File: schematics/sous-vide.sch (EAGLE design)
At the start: 27 parts, among them IC1 MEGA32-P, Q2 BC517, Q3 BC517

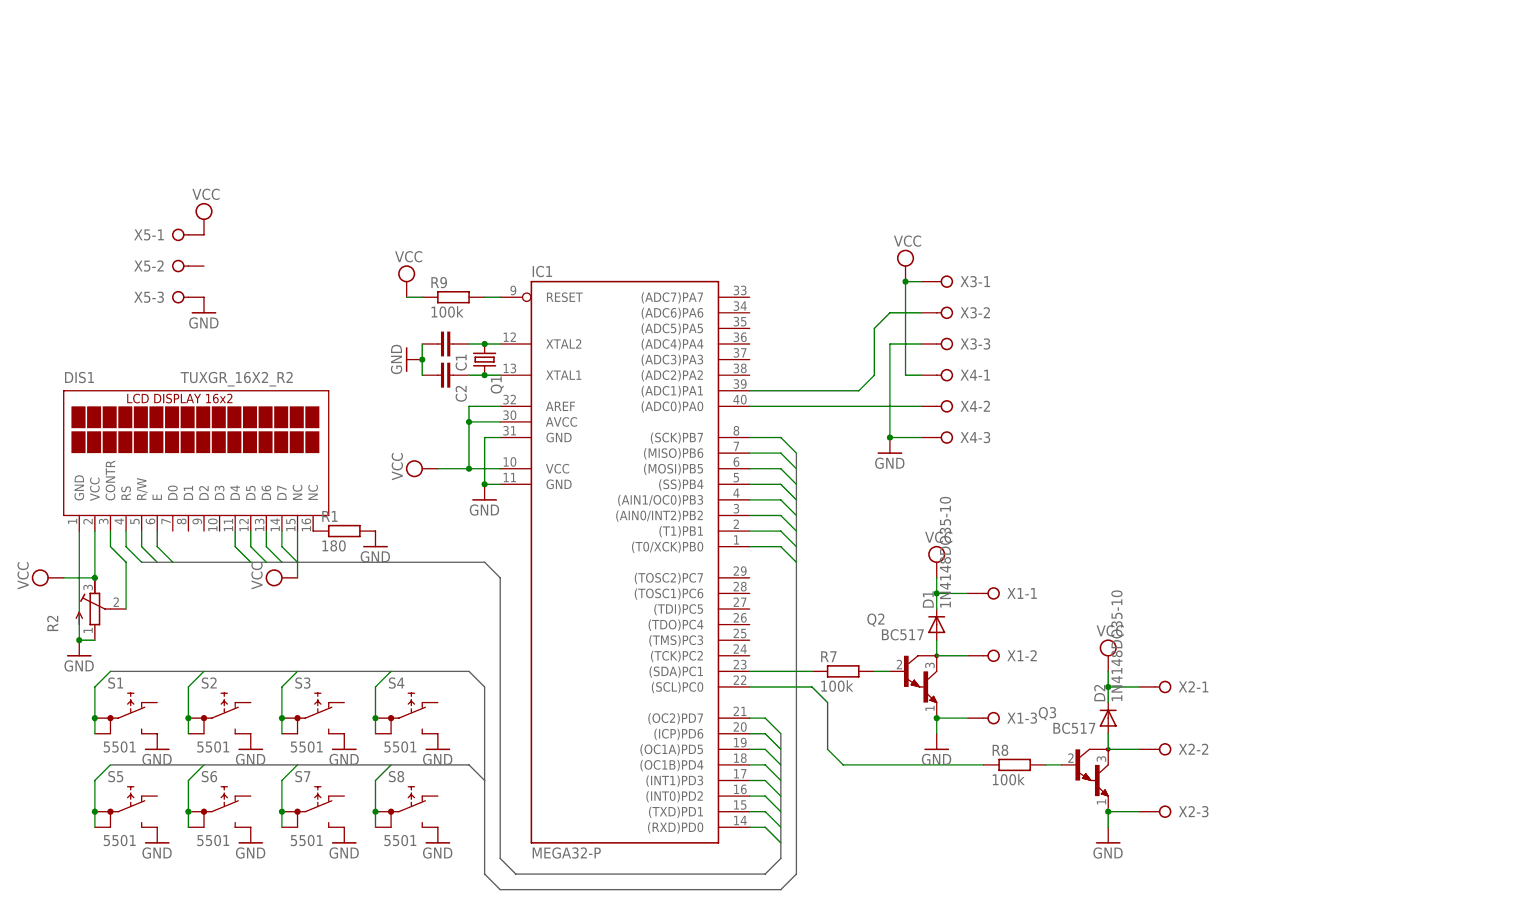
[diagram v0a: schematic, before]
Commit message: Electronic schema and board updated
Created an 8x8 cm board for cpu, display and buttons.
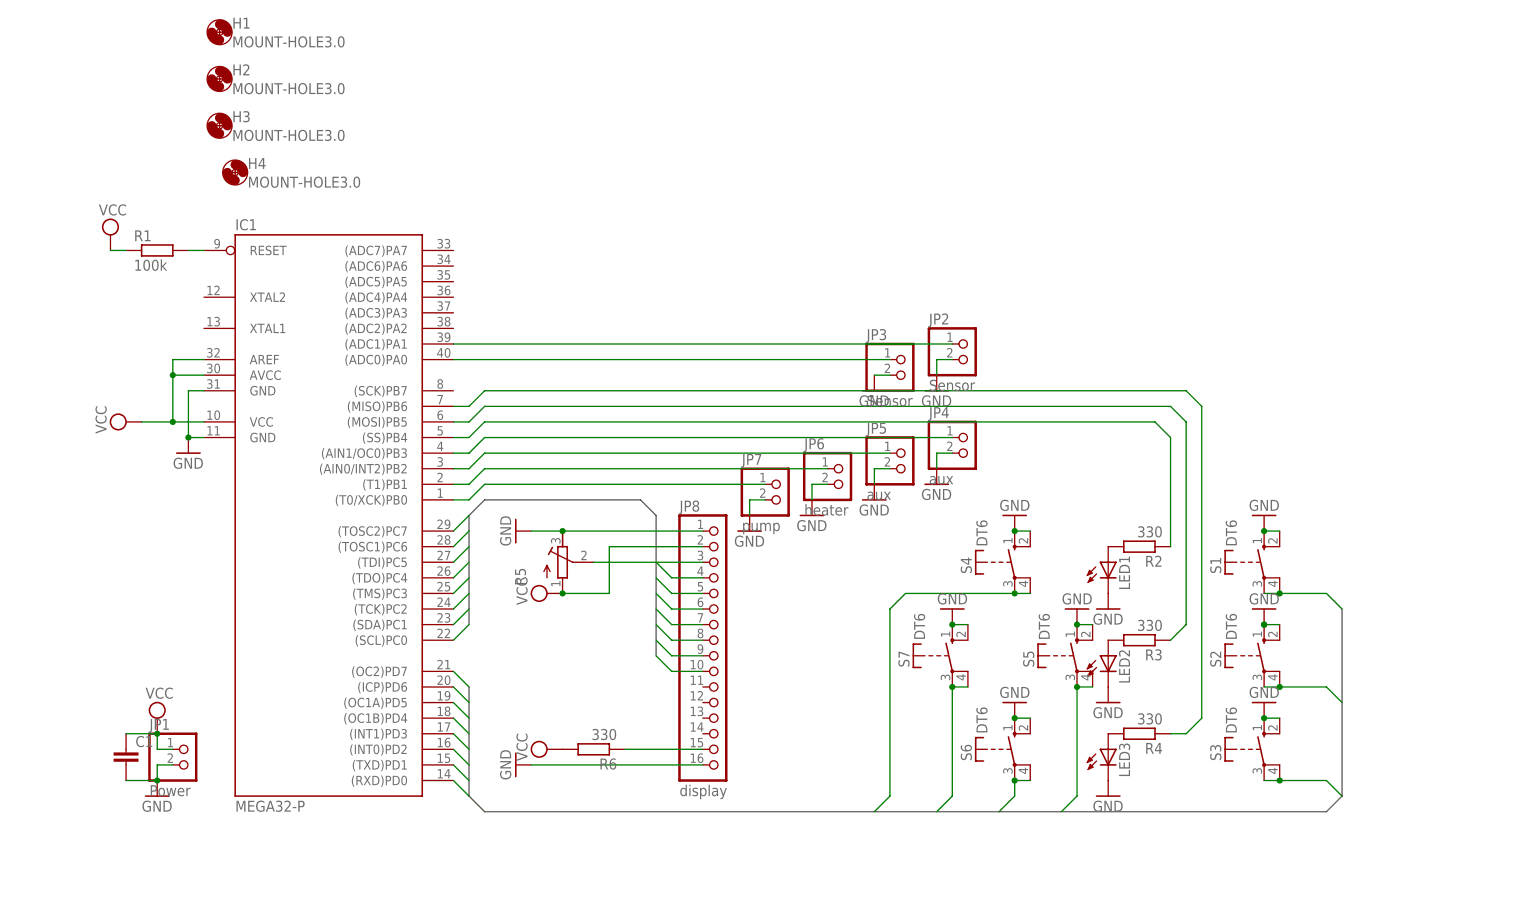
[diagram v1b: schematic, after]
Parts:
- removed C2: (no value), rcl:C-EU025-024X044
- removed D1, D2: 1N4148DO35-10, diode:1N4148DO35-10
- removed DIS1: TUXGR_16X2_R2, display-lcd:TUXGR_16X2_R2
- removed Q1: (no value), crystal:CRYSTALHC49S
- removed Q2, Q3: BC517, transistor-npn:BC517
- removed R7, R8, R9: 100k, rcl:R-EU_0207/2V
- removed S8: 5501, switch:5501
- removed X1, X2, X3, X4, X5: (no value), con-wago-508:W237-3E
- added H1, H2, H3, H4: MOUNT-HOLE3.0, holes:MOUNT-HOLE3.0
- added JP1: Power, pinhead:PINHD-1X2
- added JP2, JP3: Sensor, pinhead:PINHD-1X2
- added JP4, JP5: aux, pinhead:PINHD-1X2
- added JP6: heater, pinhead:PINHD-1X2
- added JP7: pump, pinhead:PINHD-1X2
- added JP8: display, pinhead:PINHD-1X16
- added LED1, LED2, LED3: (no value), led:LED3MM
- added R3, R4, R6: 330, rcl:R-EU_0207/2V
- added R5: (no value), resistor:R-TRIMM3339P
- C1: device rcl:C-EU025-024X044 -> resistor:C-EU025-025X050
- R1: value 180 -> 100k
- R2: value (none) -> 330; device resistor:R-TRIMM3339P -> rcl:R-EU_0207/2V
- S1, S2, S3, S4, S5, S6, S7: value 5501 -> DT6; device switch:5501 -> switch-misc:DT6
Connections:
- removed net SWITCH0: IC1.(T0/XCK)PB0, S1.1A, S1.1B
- removed net SWITCH1: IC1.(T1)PB1, S2.1A, S2.1B
- removed net SWITCH2: IC1.(AIN0/INT2)PB2, S3.1A, S3.1B
- removed net SWITCH3: IC1.(AIN1/OC0)PB3, S4.1A, S4.1B
- removed net SWITCH4: IC1.(SS)PB4, S5.1A, S5.1B
- removed net SWITCH5: IC1.(MOSI)PB5, S6.1A, S6.1B
- removed net SWITCH6: IC1.(MISO)PB6, S7.1A, S7.1B
- removed net SWITCH7: IC1.(SCK)PB7, S8.1A, S8.1B
- new net BUTTON0: IC1.(RXD)PD0, S1.P, S1.P@1
- new net BUTTON1: IC1.(TXD)PD1, S2.P, S2.P@1
- new net BUTTON2: IC1.(INT0)PD2, S3.P, S3.P@1
- new net BUTTON3: IC1.(INT1)PD3, S4.P, S4.P@1
- new net BUTTON4: IC1.(OC1B)PD4, S5.P, S5.P@1
- new net BUTTON5: IC1.(OC1A)PD5, S6.P, S6.P@1
- new net BUTTON6: IC1.(ICP)PD6, S7.P, S7.P@1
- new net BUTTON7: IC1.(OC2)PD7
- new net N$14: JP8.3, R5.S
- new net N$15: JP8.15, R6.1
- net DISPLAY0: now also IC1.(SCL)PC0; no longer DIS1.RS, IC1.(RXD)PD0
- net DISPLAY1: now also IC1.(SDA)PC1, JP8.4; no longer DIS1.R/W, IC1.(TXD)PD1
- net DISPLAY2: now also IC1.(TCK)PC2, JP8.5; no longer DIS1.E, IC1.(INT0)PD2
- net DISPLAY3: now also IC1.(TMS)PC3, JP8.6; no longer DIS1.D4, IC1.(INT1)PD3
- net DISPLAY4: now also IC1.(TDO)PC4, JP8.7; no longer DIS1.D5, IC1.(OC1B)PD4
- net DISPLAY5: now also IC1.(TDI)PC5, JP8.8; no longer DIS1.D6, IC1.(OC1A)PD5
- net DISPLAY6: now also IC1.(TOSC1)PC6, JP8.9; no longer DIS1.D7, IC1.(ICP)PD6
- net DISPLAY7: now also IC1.(TOSC2)PC7, JP8.10; no longer IC1.(OC2)PD7
- net GND: now also JP1.2, JP2.2, JP3.2, JP4.2, JP5.2, JP6.2, JP7.2, JP8.1, JP8.16, LED1.C, LED2.C, LED3.C, R5.A, S1.S, S1.S@1, S2.S, S2.S@1, S3.S, S3.S@1, S4.S, S4.S@1, S5.S, S5.S@1, S6.S, S6.S@1, S7.S, S7.S@1; no longer C2.2, DIS1.GND, Q2.E, Q3.E, R1.2, R2.E, S1.NO, S2.NO, S3.NO, S4.NO, S5.NO, S6.NO, S7.NO, S8.NO, X1-3.KL, X2-3.KL, X3-3.KL, X4-3.KL, X5-3.KL
- net N$1: now also IC1.(T0/XCK)PB0, JP7.1; no longer C1.1, IC1.XTAL2, Q1.1
- net N$10: now also IC1.(SS)PB4, R2.1; no longer Q3.B, R8.2
- net N$11: now also IC1.(MOSI)PB5, R3.1; no longer IC1.(ADC1)PA1, X3-2.KL
- net N$12: now also JP3.1; no longer X4-2.KL
- net N$13: now also IC1.(MISO)PB6, R4.1; no longer DIS1.CONTR, R2.S
- net N$2: now also IC1.(T1)PB1, JP6.1; no longer C2.1, IC1.XTAL1, Q1.2
- net N$3: now also R1.2; no longer R9.2
- net N$4: now also IC1.(AIN0/INT2)PB2, JP5.1; no longer D2.A, Q3.C, X2-2.KL
- net N$5: now also IC1.(AIN1/OC0)PB3, JP4.1; no longer DIS1.NC@2, R1.1
- net N$6: now also IC1.(ADC1)PA1, JP2.1; no longer IC1.(SCL)PC0, R8.1
- net N$7: now also LED3.A, R4.2; no longer IC1.(SDA)PC1, R7.1
- net N$8: now also LED2.A, R3.2; no longer Q2.B, R7.2
- net N$9: now also LED1.A, R2.2; no longer D1.A, Q2.C, X1-2.KL
- net VCC: now also C1.1, JP1.1, JP8.2, R1.1, R5.E, R6.2; no longer D1.C, D2.C, DIS1.NC@1, DIS1.VCC, R2.A, R9.1, X1-1.KL, X2-1.KL, X3-1.KL, X4-1.KL, X5-1.KL
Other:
- moved on the sheet: C1, IC1, R1

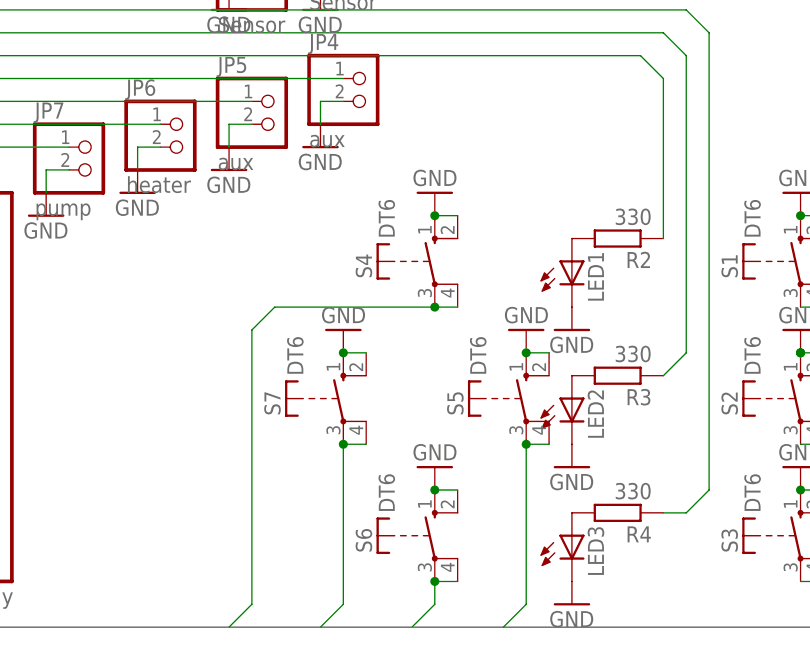
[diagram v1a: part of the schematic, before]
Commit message: Optimized PCB
Optimized PCB with easier traces for buttons.
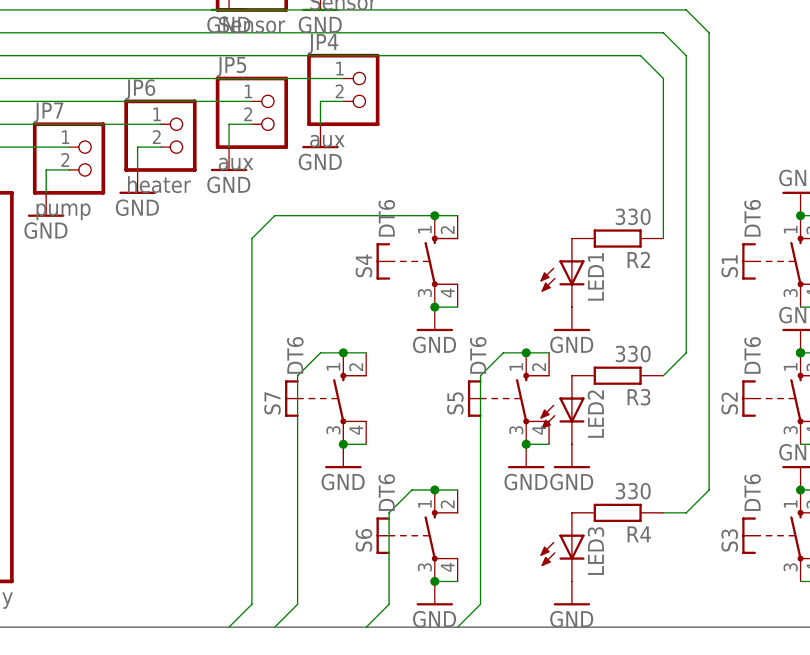
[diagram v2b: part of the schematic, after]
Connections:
- net BUTTON3: now also S4.S, S4.S@1; no longer S4.P, S4.P@1
- net BUTTON4: now also S5.S, S5.S@1; no longer S5.P, S5.P@1
- net BUTTON5: now also S6.S, S6.S@1; no longer S6.P, S6.P@1
- net BUTTON6: now also S7.S, S7.S@1; no longer S7.P, S7.P@1
- net GND: now also S4.P, S4.P@1, S5.P, S5.P@1, S6.P, S6.P@1, S7.P, S7.P@1; no longer S4.S, S4.S@1, S5.S, S5.S@1, S6.S, S6.S@1, S7.S, S7.S@1
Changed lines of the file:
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@@
 <part name="GND2" library="supply1" deviceset="GND" device=""/>
 <part name="GND3" library="supply1" deviceset="GND" device=""/>
-<part name="GND4" library="supply1" deviceset="GND" device=""/>
-<part name="GND5" library="supply1" deviceset="GND" device=""/>
-<part name="GND6" library="supply1" deviceset="GND" device=""/>
-<part name="GND7" library="supply1" deviceset="GND" device=""/>
 <part name="GND8" library="supply1" deviceset="GND" device=""/>
 <part name="JP7" library="pinhead" deviceset="PINHD-1X2" device="" value="pump"/>
@@
 <part name="H3" library="holes" deviceset="MOUNT-HOLE" device="3.0"/>
 <part name="H4" library="holes" deviceset="MOUNT-HOLE" device="3.0"/>
+<part name="GND4" library="supply1" deviceset="GND" device=""/>
+<part name="GND5" library="supply1" deviceset="GND" device=""/>
+<part name="GND6" library="supply1" deviceset="GND" device=""/>
+<part name="GND7" library="supply1" deviceset="GND" device=""/>
 </parts>
 <sheets>
@@
 <instance part="GND2" gate="1" x="190.5" y="38.1" rot="R180"/>
 <instance part="GND3" gate="1" x="190.5" y="22.86" rot="R180"/>
-<instance part="GND4" gate="1" x="149.86" y="53.34" rot="R180"/>
-<instance part="GND5" gate="1" x="160.02" y="38.1" rot="R180"/>
-<instance part="GND6" gate="1" x="149.86" y="22.86" rot="R180"/>
-<instance part="GND7" gate="1" x="139.7" y="38.1" rot="R180"/>
 <instance part="GND8" gate="1" x="15.24" y="63.5"/>
 <instance part="JP7" gate="G$1" x="111.76" y="55.88"/>
@@
 <instance part="H3" gate="G$1" x="20.32" y="116.84"/>
 <instance part="H4" gate="G$1" x="22.86" y="109.22"/>
+<instance part="GND4" gate="1" x="149.86" y="38.1"/>
+<instance part="GND5" gate="1" x="139.7" y="22.86"/>
+<instance part="GND6" gate="1" x="160.02" y="22.86"/>
+<instance part="GND7" gate="1" x="149.86" y="7.62"/>
 </instances>
 <busses>
@@
 </segment>
 <segment>
-<pinref part="S4" gate="1" pin="S"/>
-<pinref part="GND4" gate="1" pin="GND"/>
-<pinref part="S4" gate="1" pin="S@1"/>
-<wire x1="152.4" y1="50.8" x2="149.86" y2="50.8" width="0.1524" layer="91"/>
-<junction x="149.86" y="50.8"/>
-</segment>
-<segment>
-<pinref part="S5" gate="1" pin="S"/>
-<pinref part="GND5" gate="1" pin="GND"/>
-<junction x="160.02" y="35.56"/>
-<pinref part="S5" gate="1" pin="S@1"/>
-<wire x1="160.02" y1="35.56" x2="162.56" y2="35.56" width="0.1524" layer="91"/>
-</segment>
-<segment>
-<pinref part="S6" gate="1" pin="S"/>
-<pinref part="GND6" gate="1" pin="GND"/>
-<junction x="149.86" y="20.32"/>
-<pinref part="S6" gate="1" pin="S@1"/>
-<wire x1="149.86" y1="20.32" x2="152.4" y2="20.32" width="0.1524" layer="91"/>
-</segment>
-<segment>
-<pinref part="S7" gate="1" pin="S"/>
-<pinref part="GND7" gate="1" pin="GND"/>
-<junction x="139.7" y="35.56"/>
-<pinref part="S7" gate="1" pin="S@1"/>
-<wire x1="139.7" y1="35.56" x2="142.24" y2="35.56" width="0.1524" layer="91"/>
-</segment>
-<segment>
 <pinref part="IC1" gate="G$1" pin="GND@1"/>
 <wire x1="17.78" y1="73.66" x2="15.24" y2="73.66" width="0.1524" layer="91"/>
@@
 <pinref part="GND20" gate="1" pin="GND"/>
 <wire x1="99.06" y1="12.7" x2="71.12" y2="12.7" width="0.1524" layer="91"/>
+</segment>
+<segment>
+<pinref part="S4" gate="1" pin="P"/>
+<pinref part="GND4" gate="1" pin="GND"/>
+<pinref part="S4" gate="1" pin="P@1"/>
+<wire x1="152.4" y1="40.64" x2="149.86" y2="40.64" width="0.1524" layer="91"/>
+<junction x="149.86" y="40.64"/>
+</segment>
+<segment>
+<pinref part="S7" gate="1" pin="P"/>
+<pinref part="GND5" gate="1" pin="GND"/>
+<pinref part="S7" gate="1" pin="P@1"/>
+<wire x1="142.24" y1="25.4" x2="139.7" y2="25.4" width="0.1524" layer="91"/>
+<junction x="139.7" y="25.4"/>
+</segment>
+<segment>
+<pinref part="S5" gate="1" pin="P"/>
+<pinref part="GND6" gate="1" pin="GND"/>
+<pinref part="S5" gate="1" pin="P@1"/>
+<wire x1="162.56" y1="25.4" x2="160.02" y2="25.4" width="0.1524" layer="91"/>
+<junction x="160.02" y="25.4"/>
+</segment>
+<segment>
+<pinref part="S6" gate="1" pin="P"/>
+<pinref part="GND7" gate="1" pin="GND"/>
+<pinref part="S6" gate="1" pin="P@1"/>
+<wire x1="152.4" y1="10.16" x2="149.86" y2="10.16" width="0.1524" layer="91"/>
+<junction x="149.86" y="10.16"/>
 </segment>
 </net>
@@
 </segment>
 <segment>
-<wire x1="147.32" y1="5.08" x2="149.86" y2="7.62" width="0.1524" layer="91"/>
-<pinref part="S6" gate="1" pin="P"/>
-<wire x1="149.86" y1="7.62" x2="149.86" y2="10.16" width="0.1524" layer="91"/>
-<pinref part="S6" gate="1" pin="P@1"/>
-<wire x1="152.4" y1="10.16" x2="149.86" y2="10.16" width="0.1524" layer="91"/>
-<junction x="149.86" y="10.16"/>
+<wire x1="142.24" y1="5.08" x2="144.78" y2="7.62" width="0.1524" layer="91"/>
+<wire x1="144.78" y1="7.62" x2="144.78" y2="17.78" width="0.1524" layer="91"/>
+<wire x1="144.78" y1="17.78" x2="147.32" y2="20.32" width="0.1524" layer="91"/>
+<pinref part="S6" gate="1" pin="S@1"/>
+<wire x1="147.32" y1="20.32" x2="149.86" y2="20.32" width="0.1524" layer="91"/>
+<pinref part="S6" gate="1" pin="S"/>
+<junction x="149.86" y="20.32"/>
+<wire x1="149.86" y1="20.32" x2="152.4" y2="20.32" width="0.1524" layer="91"/>
 </segment>
 </net>
@@
 </segment>
 <segment>
-<wire x1="137.16" y1="5.08" x2="139.7" y2="7.62" width="0.1524" layer="91"/>
-<pinref part="S7" gate="1" pin="P"/>
-<wire x1="139.7" y1="7.62" x2="139.7" y2="25.4" width="0.1524" layer="91"/>
-<pinref part="S7" gate="1" pin="P@1"/>
-<wire x1="139.7" y1="25.4" x2="142.24" y2="25.4" width="0.1524" layer="91"/>
-<junction x="139.7" y="25.4"/>
+<wire x1="132.08" y1="5.08" x2="134.62" y2="7.62" width="0.1524" layer="91"/>
+<wire x1="134.62" y1="7.62" x2="134.62" y2="33.02" width="0.1524" layer="91"/>
+<wire x1="134.62" y1="33.02" x2="137.16" y2="35.56" width="0.1524" layer="91"/>
+<pinref part="S7" gate="1" pin="S@1"/>
+<wire x1="137.16" y1="35.56" x2="139.7" y2="35.56" width="0.1524" layer="91"/>
+<pinref part="S7" gate="1" pin="S"/>
+<junction x="139.7" y="35.56"/>
+<wire x1="139.7" y1="35.56" x2="142.24" y2="35.56" width="0.1524" layer="91"/>
 </segment>
 </net>
@@
 </segment>
 <segment>
-<wire x1="157.48" y1="5.08" x2="160.02" y2="7.62" width="0.1524" layer="91"/>
-<wire x1="160.02" y1="7.62" x2="160.02" y2="25.4" width="0.1524" layer="91"/>
-<pinref part="S5" gate="1" pin="P@1"/>
-<pinref part="S5" gate="1" pin="P"/>
-<junction x="160.02" y="25.4"/>
-<wire x1="160.02" y1="25.4" x2="162.56" y2="25.4" width="0.1524" layer="91"/>
+<wire x1="152.4" y1="5.08" x2="154.94" y2="7.62" width="0.1524" layer="91"/>
+<wire x1="154.94" y1="7.62" x2="154.94" y2="33.02" width="0.1524" layer="91"/>
+<wire x1="154.94" y1="33.02" x2="157.48" y2="35.56" width="0.1524" layer="91"/>
+<pinref part="S5" gate="1" pin="S@1"/>
+<wire x1="157.48" y1="35.56" x2="160.02" y2="35.56" width="0.1524" layer="91"/>
+<pinref part="S5" gate="1" pin="S"/>
+<junction x="160.02" y="35.56"/>
+<wire x1="160.02" y1="35.56" x2="162.56" y2="35.56" width="0.1524" layer="91"/>
 </segment>
 </net>
@@
 </segment>
 <segment>
-<wire x1="129.54" y1="38.1" x2="132.08" y2="40.64" width="0.1524" layer="91"/>
-<pinref part="S4" gate="1" pin="P"/>
-<wire x1="132.08" y1="40.64" x2="149.86" y2="40.64" width="0.1524" layer="91"/>
-<pinref part="S4" gate="1" pin="P@1"/>
-<wire x1="152.4" y1="40.64" x2="149.86" y2="40.64" width="0.1524" layer="91"/>
-<junction x="149.86" y="40.64"/>
-<wire x1="129.54" y1="38.1" x2="129.54" y2="7.62" width="0.1524" layer="91"/>
+<wire x1="129.54" y1="48.26" x2="129.54" y2="7.62" width="0.1524" layer="91"/>
 <wire x1="129.54" y1="7.62" x2="127" y2="5.08" width="0.1524" layer="91"/>
-</segment>
-</net>
+<pinref part="S4" gate="1" pin="S@1"/>
+<pinref part="S4" gate="1" pin="S"/>
+<wire x1="152.4" y1="50.8" x2="149.86" y2="50.8" width="0.1524" layer="91"/>
+<wire x1="149.86" y1="50.8" x2="132.08" y2="50.8" width="0.1524" layer="91"/>
+<wire x1="132.08" y1="50.8" x2="129.54" y2="48.26" width="0.1524" layer="91"/>
+<junction x="149.86" y="50.8"/>
+</segment>
+</net>
